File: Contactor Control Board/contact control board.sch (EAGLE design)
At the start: 35 parts, among them Q1 2n2222, Q2 2n2222, Q3 2n2222, Q4 MOSFET-NCHANNELFQP30N06L, U1 MM74HC125N

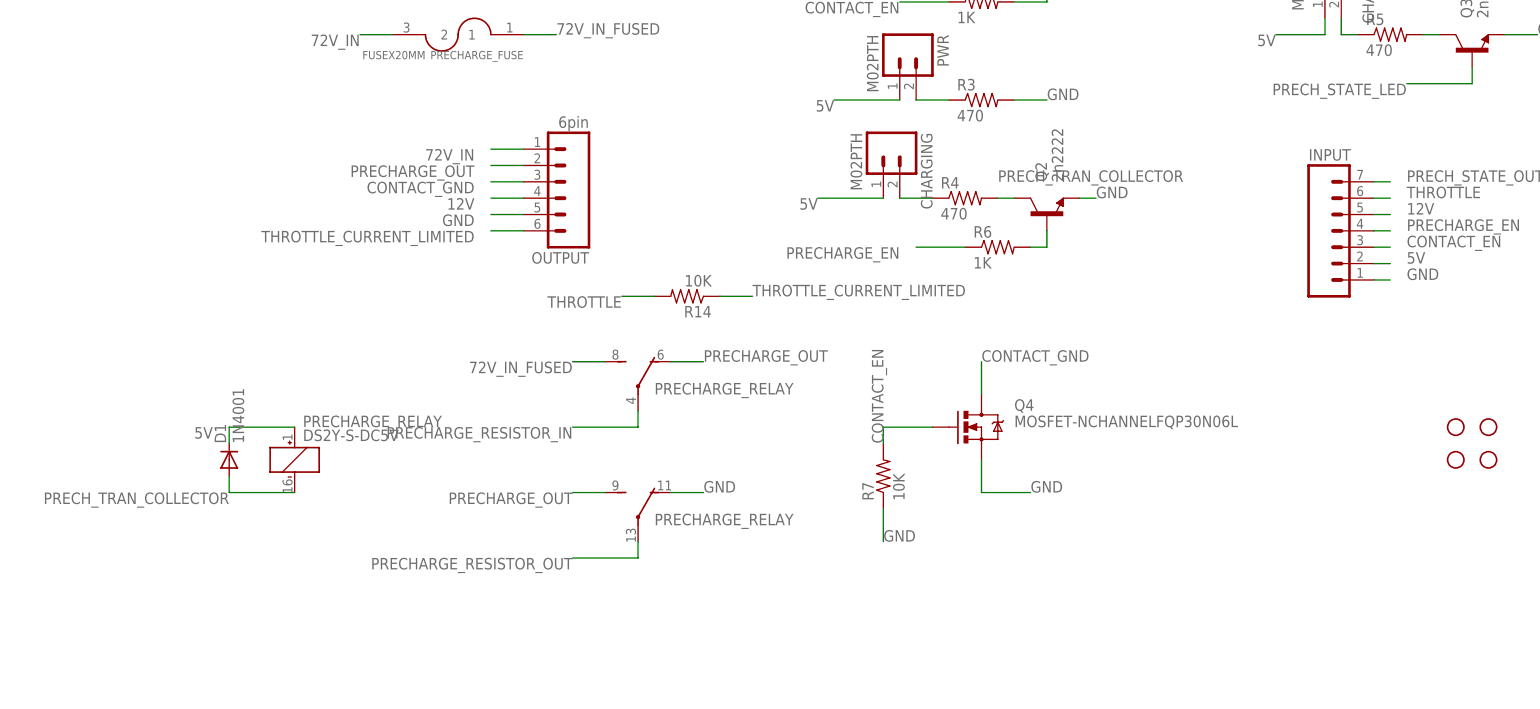
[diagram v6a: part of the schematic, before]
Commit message: Updated precharge design
Replaced transistor with a FET as the Arduino can't source enough
current to trigger both the relay and the LED... At least not with the
transistors which were specced.
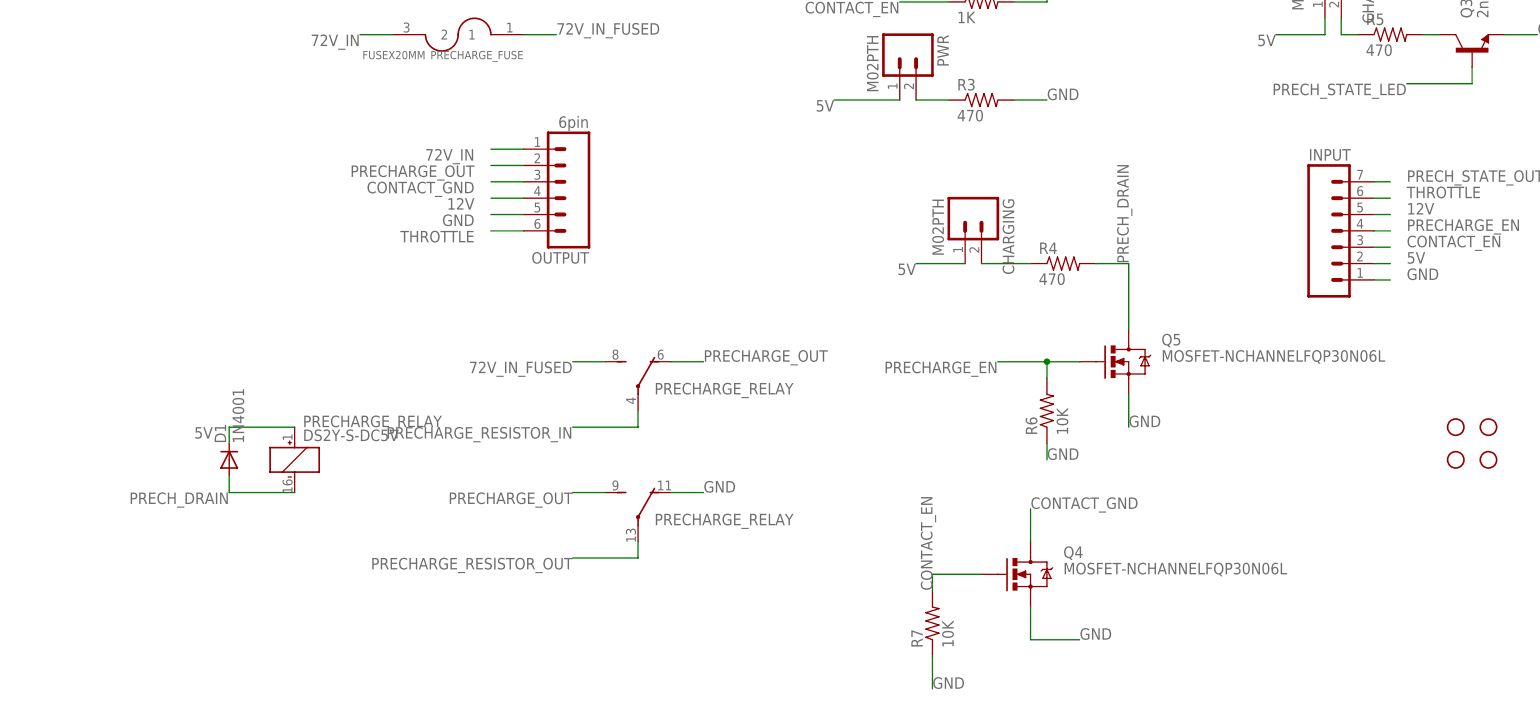
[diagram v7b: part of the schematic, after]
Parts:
- removed Q2: 2n2222, SparkFun-DiscreteSemi:TRANSISTOR_NPNTO-92-AMMO
- removed R14: 10K, SparkFun-Resistors:RESISTORPTH-1/4W
- added Q5: MOSFET-NCHANNELFQP30N06L, SparkFun-DiscreteSemi:MOSFET-NCHANNELFQP30N06L
- R6: value 1K -> 10K
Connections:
- removed net PRECH_TRAN_COLLECTOR: D1.A, PRECHARGE_RELAY1.-, Q2.C, R4.2
- removed net PRECH_TRAN_IN: Q2.B, R6.2
- removed net THROTTLE_CURRENT_LIMITED: OUTPUT.6, R14.1
- new net PRECH_DRAIN: D1.A, PRECHARGE_RELAY1.-, Q5.D, R4.2
- net GND: now also Q5.S, R6.1; no longer Q2.E
- net PRECHARGE_EN: now also Q5.G, R6.2; no longer R6.1
- net THROTTLE: now also OUTPUT.6; no longer R14.2
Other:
- moved on the sheet: CHARGING, Q4, R4, R6, R7
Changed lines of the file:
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@@
 <part name="R3" library="SparkFun-Resistors" deviceset="RESISTOR" device="PTH-1/4W" value="470"/>
 <part name="R4" library="SparkFun-Resistors" deviceset="RESISTOR" device="PTH-1/4W" value="470"/>
-<part name="R6" library="SparkFun-Resistors" deviceset="RESISTOR" device="PTH-1/4W" value="1K"/>
 <part name="R7" library="SparkFun-Resistors" deviceset="RESISTOR" device="PTH-1/4W" value="10K"/>
 <part name="Q4" library="SparkFun-DiscreteSemi" deviceset="MOSFET-NCHANNEL" device="FQP30N06L"/>
@@
 <part name="CHARGED" library="SparkFun-Connectors" deviceset="M02" device="PTH"/>
 <part name="R5" library="SparkFun-Resistors" deviceset="RESISTOR" device="PTH-1/4W" value="470"/>
-<part name="R14" library="SparkFun-Resistors" deviceset="RESISTOR" device="PTH-1/4W" value="10K"/>
 <part name="R15" library="SparkFun-Resistors" deviceset="RESISTOR" device="PTH-1/4W" value="1k"/>
 <part name="U1" library="mm74hc125n" deviceset="MM74HC125N" device=""/>
 <part name="Q3" library="SparkFun-DiscreteSemi" deviceset="TRANSISTOR_NPN" device="TO-92-AMMO" value="2n2222"/>
 <part name="Q1" library="SparkFun-DiscreteSemi" deviceset="TRANSISTOR_NPN" device="TO-92-AMMO" value="2n2222"/>
-<part name="Q2" library="SparkFun-DiscreteSemi" deviceset="TRANSISTOR_NPN" device="TO-92-AMMO" value="2n2222"/>
+<part name="Q5" library="SparkFun-DiscreteSemi" deviceset="MOSFET-NCHANNEL" device="FQP30N06L"/>
+<part name="R6" library="SparkFun-Resistors" deviceset="RESISTOR" device="PTH-1/4W" value="10K"/>
 </parts>
 <sheets>
@@
 <instance part="R2" gate="G$1" x="63.5" y="91.44"/>
 <instance part="R3" gate="G$1" x="66.04" y="68.58"/>
-<instance part="R4" gate="G$1" x="63.5" y="53.34"/>
-<instance part="R6" gate="G$1" x="68.58" y="45.72"/>
-<instance part="R7" gate="G$1" x="50.8" y="10.16" rot="R90"/>
-<instance part="Q4" gate="G$1" x="66.04" y="17.78"/>
+<instance part="R4" gate="G$1" x="78.74" y="43.18"/>
+<instance part="R7" gate="G$1" x="58.42" y="-12.7" rot="R90"/>
+<instance part="Q4" gate="G$1" x="73.66" y="-5.08"/>
 <instance part="D1" gate="G$1" x="-50.8" y="12.7" rot="R90"/>
 <instance part="OUTPUT" gate="G$1" x="0" y="55.88" rot="R180"/>
@@
 <instance part="ACTIVE" gate="G$1" x="50.8" y="99.06" rot="R270"/>
 <instance part="PWR" gate="G$1" x="53.34" y="76.2" rot="R270"/>
-<instance part="CHARGING" gate="G$1" x="50.8" y="60.96" rot="R270"/>
+<instance part="CHARGING" gate="G$1" x="63.5" y="50.8" rot="R270"/>
 <instance part="RESISTOR" gate="G$1" x="53.34" y="114.3" rot="R180"/>
 <instance part="R8" gate="G$1" x="71.12" y="160.02" rot="R270"/>
@@
 <instance part="CHARGED" gate="G$1" x="119.38" y="88.9" rot="R270"/>
 <instance part="R5" gate="G$1" x="129.54" y="78.74"/>
-<instance part="R14" gate="G$1" x="20.32" y="38.1" rot="R180"/>
 <instance part="R15" gate="G$1" x="276.86" y="93.98" rot="R90"/>
 <instance part="U1" gate="A" x="241.3" y="91.44"/>
 <instance part="Q3" gate="G$1" x="142.24" y="76.2" rot="R90"/>
 <instance part="Q1" gate="G$1" x="76.2" y="88.9" rot="R90"/>
-<instance part="Q2" gate="G$1" x="76.2" y="50.8" rot="R90"/>
+<instance part="Q5" gate="G$1" x="88.9" y="27.94"/>
+<instance part="R6" gate="G$1" x="76.2" y="20.32" rot="R90"/>
 </instances>
 <busses>
@@
 </segment>
 <segment>
-<pinref part="CHARGING" gate="G$1" pin="1"/>
-<wire x1="50.8" y1="53.34" x2="40.64" y2="53.34" width="0.2032" layer="91"/>
-<label x="40.64" y="53.34" size="1.778" layer="95" rot="R180"/>
-</segment>
-<segment>
 <pinref part="D1" gate="G$1" pin="C"/>
 <wire x1="-40.64" y1="17.78" x2="-50.8" y2="17.78" width="0.2032" layer="91"/>
@@
 <pinref part="U1" gate="A" pin="VCC"/>
 </segment>
+<segment>
+<pinref part="CHARGING" gate="G$1" pin="1"/>
+<wire x1="63.5" y1="43.18" x2="55.88" y2="43.18" width="0.2032" layer="91"/>
+<label x="55.88" y="43.18" size="1.778" layer="95" rot="R180"/>
+</segment>
 </net>
 <net name="GND" class="0">
 <segment>
 <pinref part="R7" gate="G$1" pin="1"/>
-<wire x1="50.8" y1="5.08" x2="50.8" y2="0" width="0.2032" layer="91"/>
-<label x="50.8" y="0" size="1.778" layer="95"/>
+<wire x1="58.42" y1="-17.78" x2="58.42" y2="-22.86" width="0.2032" layer="91"/>
+<label x="58.42" y="-22.86" size="1.778" layer="95"/>
 </segment>
 <segment>
@@
 <segment>
 <pinref part="Q4" gate="G$1" pin="S"/>
-<wire x1="66.04" y1="12.7" x2="66.04" y2="7.62" width="0.2032" layer="91"/>
-<wire x1="66.04" y1="7.62" x2="73.66" y2="7.62" width="0.2032" layer="91"/>
-<label x="73.66" y="7.62" size="1.778" layer="95"/>
-</segment>
-<segment>
-<wire x1="81.28" y1="53.34" x2="83.82" y2="53.34" width="0.2032" layer="91"/>
-<label x="83.82" y="53.34" size="1.778" layer="95"/>
-<pinref part="Q2" gate="G$1" pin="E"/>
+<wire x1="73.66" y1="-10.16" x2="73.66" y2="-15.24" width="0.2032" layer="91"/>
+<wire x1="73.66" y1="-15.24" x2="81.28" y2="-15.24" width="0.2032" layer="91"/>
+<label x="81.28" y="-15.24" size="1.778" layer="95"/>
 </segment>
 <segment>
@@
 <label x="218.44" y="73.66" size="1.778" layer="95" rot="R180"/>
 </segment>
+<segment>
+<pinref part="Q5" gate="G$1" pin="S"/>
+<wire x1="88.9" y1="22.86" x2="88.9" y2="17.78" width="0.2032" layer="91"/>
+<label x="88.9" y="17.78" size="1.778" layer="95"/>
+</segment>
+<segment>
+<pinref part="R6" gate="G$1" pin="1"/>
+<wire x1="76.2" y1="15.24" x2="76.2" y2="12.7" width="0.2032" layer="91"/>
+<label x="76.2" y="12.7" size="1.778" layer="95"/>
+</segment>
 </net>
 <net name="CONTACT_EN" class="0">
@@
 <pinref part="Q4" gate="G$1" pin="G"/>
 <pinref part="R7" gate="G$1" pin="2"/>
-<wire x1="58.42" y1="17.78" x2="50.8" y2="17.78" width="0.2032" layer="91"/>
-<wire x1="50.8" y1="17.78" x2="50.8" y2="15.24" width="0.2032" layer="91"/>
-<label x="50.8" y="15.24" size="1.778" layer="95" rot="R90"/>
+<wire x1="66.04" y1="-5.08" x2="58.42" y2="-5.08" width="0.2032" layer="91"/>
+<wire x1="58.42" y1="-5.08" x2="58.42" y2="-7.62" width="0.2032" layer="91"/>
+<label x="58.42" y="-7.62" size="1.778" layer="95" rot="R90"/>
 </segment>
 <segment>
@@
 <net name="PRECHARGE_EN" class="0">
 <segment>
-<pinref part="R6" gate="G$1" pin="1"/>
-<wire x1="63.5" y1="45.72" x2="55.88" y2="45.72" width="0.2032" layer="91"/>
-<label x="53.34" y="45.72" size="1.778" layer="95" rot="R180"/>
-</segment>
-<segment>
 <wire x1="127" y1="48.26" x2="129.54" y2="48.26" width="0.2032" layer="91"/>
 <label x="132.08" y="48.26" size="1.778" layer="95"/>
 <pinref part="INPUT" gate="G$1" pin="4"/>
 </segment>
+<segment>
+<pinref part="Q5" gate="G$1" pin="G"/>
+<wire x1="81.28" y1="27.94" x2="76.2" y2="27.94" width="0.2032" layer="91"/>
+<label x="68.58" y="27.94" size="1.778" layer="95" rot="R180"/>
+<pinref part="R6" gate="G$1" pin="2"/>
+<wire x1="76.2" y1="27.94" x2="68.58" y2="27.94" width="0.2032" layer="91"/>
+<wire x1="76.2" y1="25.4" x2="76.2" y2="27.94" width="0.2032" layer="91"/>
+<junction x="76.2" y="27.94"/>
+</segment>
 </net>
 <net name="12V" class="0">
@@
 </segment>
 <segment>
-<pinref part="R14" gate="G$1" pin="2"/>
-<wire x1="15.24" y1="38.1" x2="10.16" y2="38.1" width="0.2032" layer="91"/>
-<label x="10.16" y="38.1" size="1.778" layer="95" rot="R180"/>
+<pinref part="OUTPUT" gate="G$1" pin="6"/>
+<wire x1="-5.08" y1="48.26" x2="-10.16" y2="48.26" width="0.2032" layer="91"/>
+<label x="-12.7" y="48.26" size="1.778" layer="95" rot="R180"/>
 </segment>
 </net>
@@
 </segment>
 </net>
-<net name="N$14" class="0">
-<segment>
-<pinref part="R4" gate="G$1" pin="1"/>
-<pinref part="CHARGING" gate="G$1" pin="2"/>
-<wire x1="53.34" y1="53.34" x2="58.42" y2="53.34" width="0.2032" layer="91"/>
-</segment>
-</net>
 <net name="72V_IN_FUSED" class="0">
 <segment>
@@
 <segment>
 <pinref part="Q4" gate="G$1" pin="D"/>
-<wire x1="66.04" y1="22.86" x2="66.04" y2="27.94" width="0.2032" layer="91"/>
-<label x="66.04" y="27.94" size="1.778" layer="95"/>
+<wire x1="73.66" y1="0" x2="73.66" y2="5.08" width="0.2032" layer="91"/>
+<label x="73.66" y="5.08" size="1.778" layer="95"/>
 </segment>
 </net>
@@
 </segment>
 </net>
-<net name="PRECH_TRAN_COLLECTOR" class="0">
-<segment>
-<pinref part="R4" gate="G$1" pin="2"/>
-<wire x1="71.12" y1="53.34" x2="68.58" y2="53.34" width="0.1524" layer="91"/>
-<label x="68.58" y="55.88" size="1.778" layer="95"/>
-<pinref part="Q2" gate="G$1" pin="C"/>
-</segment>
+<net name="PRECH_DRAIN" class="0">
 <segment>
 <pinref part="D1" gate="G$1" pin="A"/>
@@
 <pinref part="PRECHARGE_RELAY" gate="1" pin="-"/>
 </segment>
+<segment>
+<pinref part="R4" gate="G$1" pin="2"/>
+<pinref part="Q5" gate="G$1" pin="D"/>
+<wire x1="83.82" y1="43.18" x2="88.9" y2="43.18" width="0.2032" layer="91"/>
+<wire x1="88.9" y1="43.18" x2="88.9" y2="33.02" width="0.2032" layer="91"/>
+<label x="88.9" y="43.18" size="1.778" layer="95" rot="R90"/>
+</segment>
 </net>
 <net name="PRECH_STATE_OUT" class="0">
@@
 </segment>
 </net>
-<net name="PRECH_TRAN_IN" class="0">
-<segment>
-<pinref part="R6" gate="G$1" pin="2"/>
-<wire x1="73.66" y1="45.72" x2="76.2" y2="45.72" width="0.2032" layer="91"/>
-<wire x1="76.2" y1="45.72" x2="76.2" y2="48.26" width="0.2032" layer="91"/>
-<pinref part="Q2" gate="G$1" pin="B"/>
-</segment>
-</net>
 <net name="N$4" class="0">
 <segment>
@@
 <wire x1="134.62" y1="78.74" x2="137.16" y2="78.74" width="0.2032" layer="91"/>
 <pinref part="Q3" gate="G$1" pin="C"/>
-</segment>
-</net>
-<net name="THROTTLE_CURRENT_LIMITED" class="0">
-<segment>
-<pinref part="OUTPUT" gate="G$1" pin="6"/>
-<wire x1="-5.08" y1="48.26" x2="-10.16" y2="48.26" width="0.2032" layer="91"/>
-<label x="-12.7" y="48.26" size="1.778" layer="95" rot="R180"/>
-</segment>
-<segment>
-<pinref part="R14" gate="G$1" pin="1"/>
-<wire x1="25.4" y1="38.1" x2="30.48" y2="38.1" width="0.2032" layer="91"/>
-<label x="30.48" y="38.1" size="1.778" layer="95"/>
 </segment>
 </net>
@@
 </segment>
 </net>
+<net name="N$7" class="0">
+<segment>
+<pinref part="CHARGING" gate="G$1" pin="2"/>
+<pinref part="R4" gate="G$1" pin="1"/>
+<wire x1="66.04" y1="43.18" x2="73.66" y2="43.18" width="0.2032" layer="91"/>
+</segment>
+</net>
